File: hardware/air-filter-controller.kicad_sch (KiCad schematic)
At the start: 81 parts, among them J1 TYPE-C-31-M-12, J13 Conn_01x02, J14 Conn_01x02, J15 Conn_01x03, J16 Conn_01x08, J17 Conn_01x08, J2 Conn_01x05, Q1 AO3400A, SW1 SW_Push, SW2 SW_Push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

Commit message: v1.1: start updating layout
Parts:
- removed C6: 100nF, Capacitor_SMD:C_0402_1005Metric, symbol Device:C
- removed U2: ADP2100, Homebrew:ADP2100_HandSoldering, symbol Homebrew:ADP2100
- added H5: Strain Relief, Homebrew:3_pin_2.54mm_pitch_strain_relief, symbol Mechanical:MountingHole
- D35, D37, D38, D39: value WS2812B -> WS2812B-2020; footprint Homebrew:LED-SMD_4P-L1.6-W1.5_XL-1615RGBC-WS2812B -> Homebrew:LED-SMD_4P-L2.0-W2.0-TL_WS2812B-2020
- R8: value 15k 1% -> 16k 1%; LCSC C25756 -> C25759
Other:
- note added: "12V -> "5V" switching regulator Set to 4.73V so that 3.3 >= 0.7 * VDD"
- note removed: "12V -> 5V switching regulator"
- note removed: "Differential pressure sensor"

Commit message: Hardware revision v1.1:
- Fix flipped USB lines
- Remove diode on BOOT switch
- Remove buzzer resistor
- Change voltage divider to ADC channel 1
- Increased from 9 to 10 fan channels
- Switched to addressable LEDs
- Added connector for offboard WS2812 LEDs
- Added a Qwiic connector
- Added two connectors for PMS5003 particle sensors
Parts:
- added C6: 10uF, Capacitor_SMD:C_0603_1608Metric, symbol Device:C
- J15: now not fitted
- J16, J17: footprint easyeda2kicad:CONN-TH_8P-P1.25_HCTL_HC-1.25-8A -> Homebrew:CONN-TH_8P-P1.25_HCTL_HC-1.25-8A
- J2: value Conn_01x05 -> Conn_01x06; footprint Connector_PinHeader_2.54mm:PinHeader_1x05_P2.54mm_Vertical -> Connector_PinHeader_2.54mm:PinHeader_1x06_P2.54mm_Vertical
- R48, R49, R50, R51, R52, R53: LCSC C25076 -> C22775
- U5: value ZX-SH1.0-4PWT -> HC-1.0-4PLT; footprint easyeda2kicad:CONN-SMD_4P-P1.00_MEGASTAR_ZX-SH1.0-4PWT -> Homebrew:CONN-SMD_4P-P1.00_HC-1.0-4PLT; LCSC C7430446 -> C2845372; LCSC Part C7430446 -> (none)
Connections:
- net +5V: now also C6.1
- net GND: now also C6.2
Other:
- note added: "Qwiic connector"
- moved on the sheet: C17, C18, C7, U4

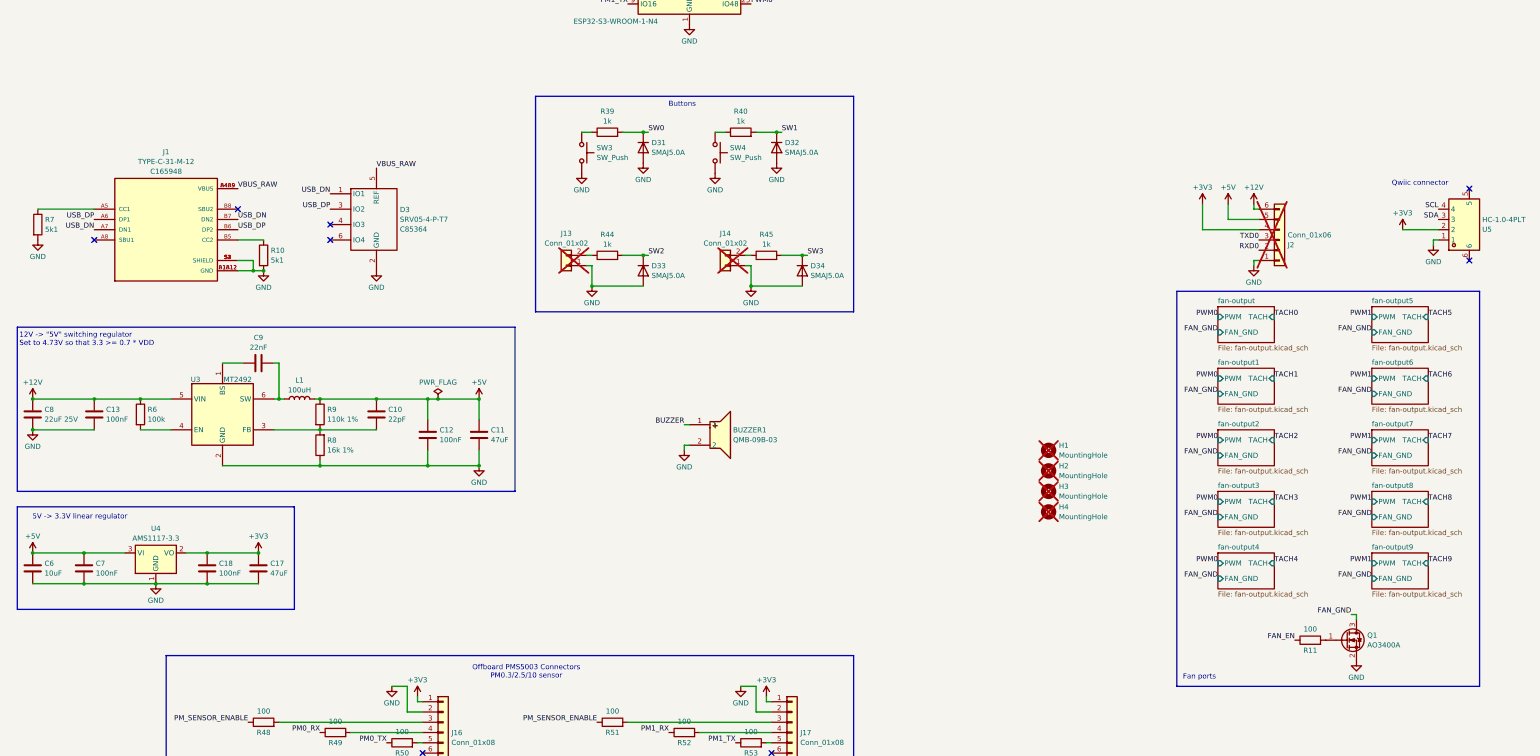
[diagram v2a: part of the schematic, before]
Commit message: WIP address conducted emissions
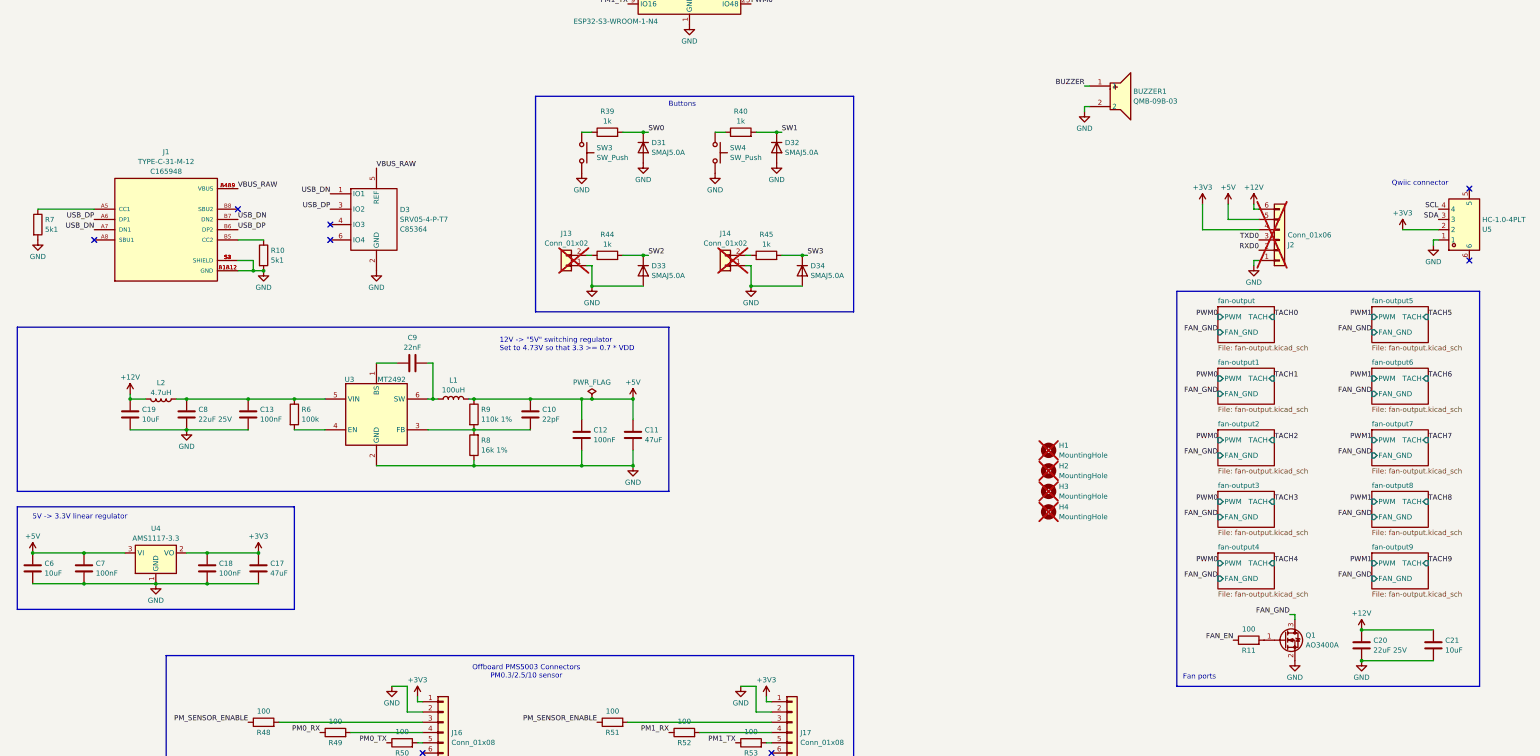
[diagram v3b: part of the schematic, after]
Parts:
- added C19, C21: 10uF, Capacitor_SMD:C_0603_1608Metric, symbol Device:C
- added C20: 22uF 25V, Capacitor_SMD:C_1206_3216Metric, symbol Device:C
- added L2: 4.7uH, Inductor_SMD:L_Sunlord_SWPA4030S, symbol Device:L
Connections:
- net +12V: now also C19.1, C20.1, C21.1, L2.2; no longer C13.1, C8.1, R6.1, U3.5 (VIN)
- net GND: now also C19.2, C20.2, C21.2
- new net: C13.1, C8.1, L2.1, R6.1, U3.5 (VIN)
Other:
- moved on the sheet: BUZZER1, C10, C11, C12, C13, C8, C9, L1, Q1, R11, R6, R8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

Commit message: Hardware v1.1
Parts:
- removed C21: 10uF, Capacitor_SMD:C_0603_1608Metric, symbol Device:C
- added C22: 220uF, Capacitor_SMD:CP_Elec_8x10, symbol Device:C_Polarized
- added C23: 22uF 25V, Capacitor_SMD:C_1206_3216Metric, symbol Device:C
- added C34: 100nF, Capacitor_SMD:C_0402_1005Metric, symbol Device:C
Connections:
- net +12V: now also C13.1, C8.1, L2.1, R6.1, U3.5 (VIN), C23.1; no longer C5.1, D1.1 (K), D2.1 (K), F1.2, L2.2
- net GND: now also C22.2, C23.2, C34.2
- new net 12V_PREFILTER: C22.1, C34.1, C5.1, D1.1 (K), D2.1 (K), F1.2, L2.2
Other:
- note added: "Pi filter for fans and buck noise"
- moved on the sheet: C1, C10, C11, C12, C13, C19, C2, C3, C4, C5, C8, C9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
